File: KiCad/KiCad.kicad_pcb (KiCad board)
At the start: 2 copper layers, 39.4 x 34.8 mm, 32 parts, among them J1 Conn_01x04_Male, J2 Conn_01x04_Male, J3 Conn_01x04_Male, J4 USB_B_Micro, SW1 SW_SPDT, U1 AMS1117-3.3, U2 STM32F103C8T6, Y1 Crystal_GND24

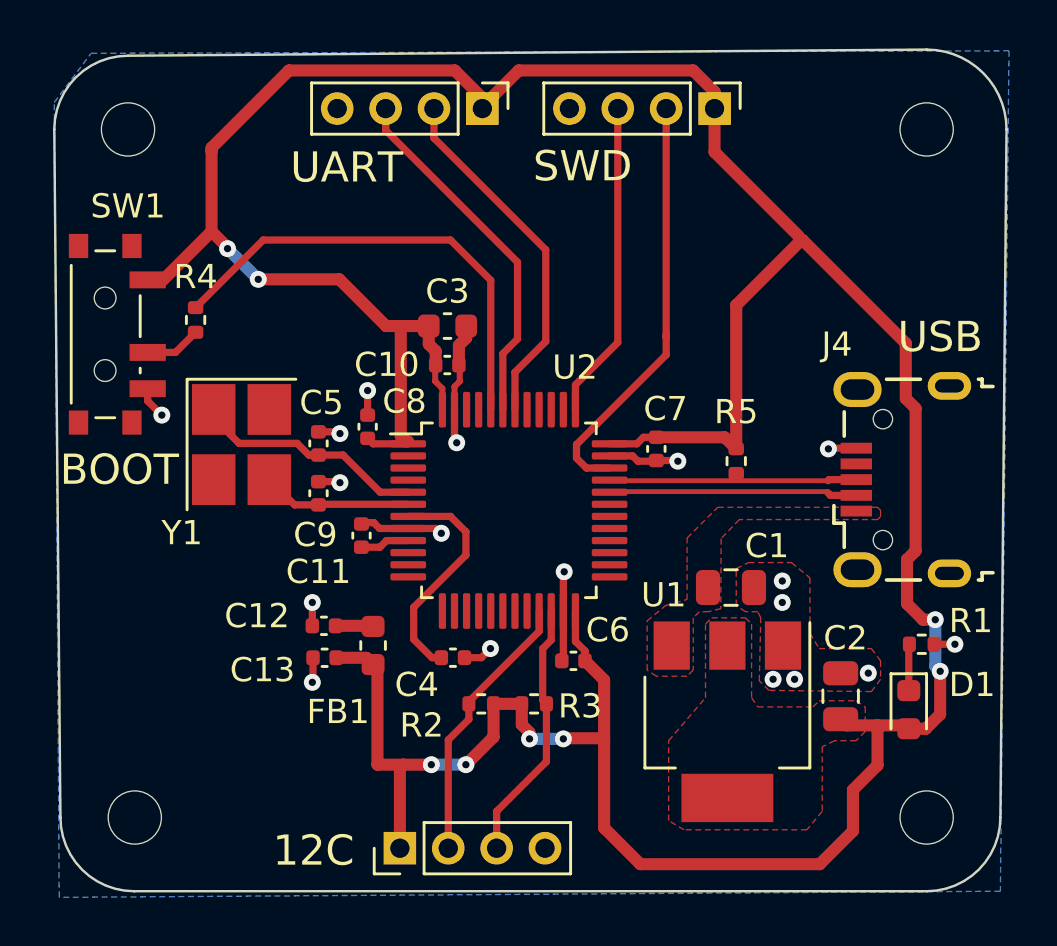
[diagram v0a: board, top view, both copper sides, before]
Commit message: Fixed some design bugs and added board title
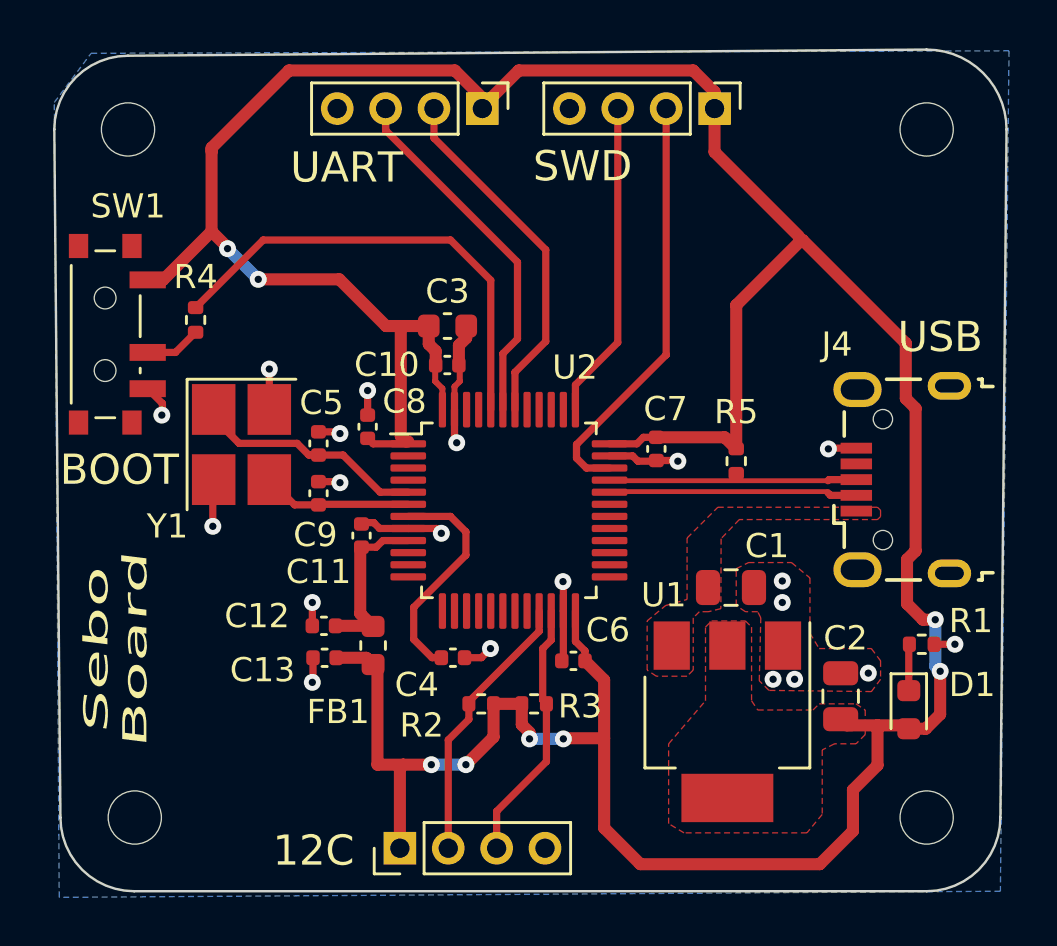
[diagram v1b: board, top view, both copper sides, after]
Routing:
- net +3.3VA: track 3.61 -> 7.13 mm
- net GND: track 24.7 -> 28.1 mm, vias 18 -> 20
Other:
- board text added: "Sebo Board"

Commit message: Sourced parts & Changed some components
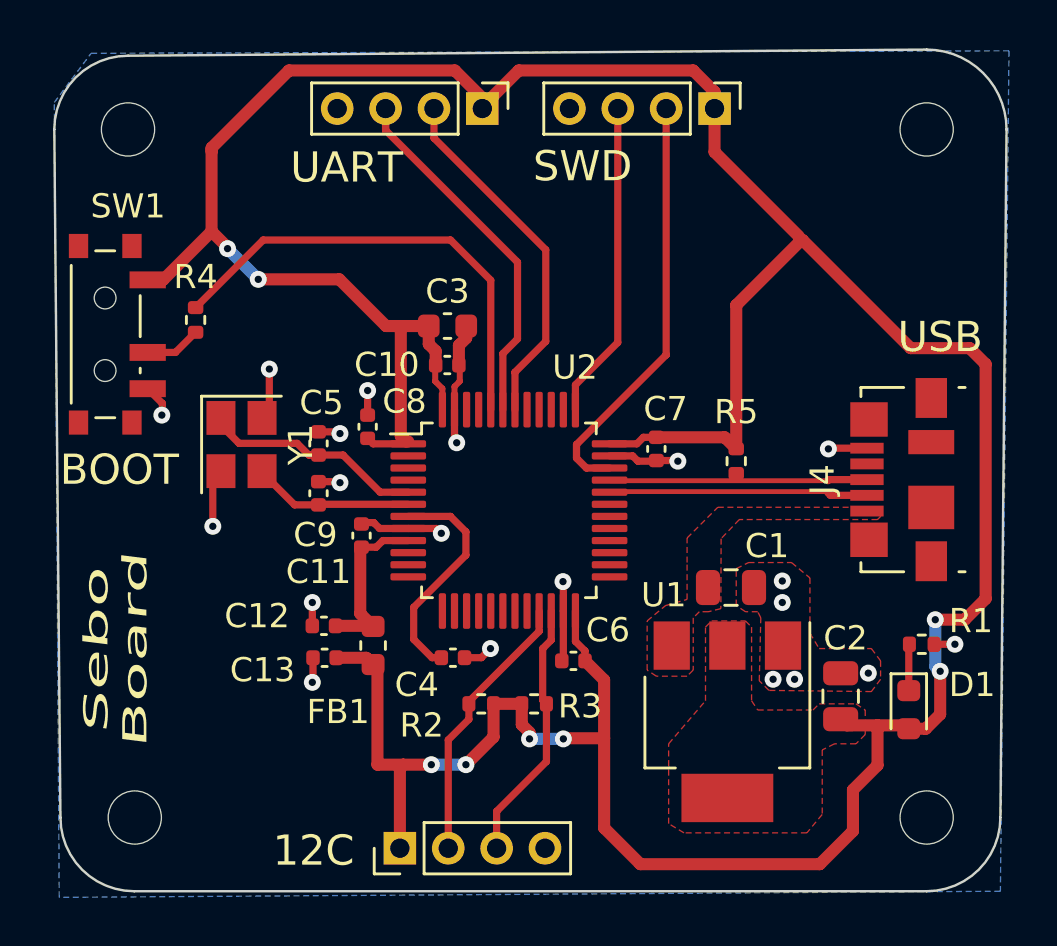
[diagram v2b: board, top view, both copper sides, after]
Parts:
- J4: footprint Connector_USB:USB_Micro-B_Wuerth_629105150521 -> Connector_USB:USB_Micro-B_Molex_47346-0001
- Y1: footprint Crystal:Crystal_SMD_3225-4Pin_3.2x2.5mm_HandSoldering -> Crystal:Crystal_SMD_3225-4Pin_3.2x2.5mm
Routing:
- net +3.3V: track 149.6 -> 152.8 mm

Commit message: Recreated the gerbers
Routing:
- net /HSE_IN: track 9.67 -> 9.10 mm
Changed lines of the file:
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@@
       (drillshape 0)
       (scaleselection 1)
-      (outputdirectory "manufacturing/")
+      (outputdirectory "manufactoringv2/gerbers/")
     )
   )
@@
     (property "Sheetname" "")
     (attr smd)
-    (fp_text reference "Y1" (at 0 -2.45 -90) (layer "F.SilkS")
+    (fp_text reference "Y1" (at 2.9232 -0.5404) (layer "F.SilkS")
       (effects (font (size 1 1) (thickness 0.15)))
     )
@@
   (segment (start 121.9745 90.158) (end 122.174 90.3575) (width 0.3) (layer "F.Cu") (net 2))
   (segment (start 122.936 83.436) (end 122.9 83.4) (width 0.25) (layer "F.Cu") (net 2))
+  (segment (start 112.762 88.138) (end 112.762 88.088) (width 0.3) (layer "F.Cu") (net 2))
   (segment (start 120.8055 90.158) (end 121.9745 90.158) (width 0.3) (layer "F.Cu") (net 2))
   (segment (start 127.218 95.568) (end 127.155 95.631) (width 0.3) (layer "F.Cu") (net 2))
@@
   (segment (start 127.218 93.5705) (end 127.218 92.3692) (width 0.3) (layer "F.Cu") (net 2))
   (segment (start 127.218 93.5705) (end 127.218 95.568) (width 0.3) (layer "F.Cu") (net 2))
-  (segment (start 112.762 88.124) (end 112.7252 88.0872) (width 0.3) (layer "F.Cu") (net 2))
+  (segment (start 112.7252 88.1248) (end 112.7252 90.0684) (width 0.3) (layer "F.Cu") (net 2))
   (segment (start 116.868 95.504) (end 116.868 96.492) (width 0.3) (layer "F.Cu") (net 2))
   (segment (start 142.5468 94.9452) (end 143.4084 94.9452) (width 0.3) (layer "F.Cu") (net 2))
@@
   (segment (start 115.062 85.238) (end 115.062 83.566) (width 0.3) (layer "F.Cu") (net 2))
   (segment (start 123.203 82.283) (end 122.9 82.586) (width 0.5) (layer "F.Cu") (net 2))
-  (segment (start 112.762 88.138) (end 112.762 88.124) (width 0.3) (layer "F.Cu") (net 2))
-  (segment (start 112.7252 88.0872) (end 112.7252 90.0684) (width 0.3) (layer "F.Cu") (net 2))
   (segment (start 131.925 87.348) (end 131.953 87.376) (width 0.3) (layer "F.Cu") (net 2))
   (segment (start 119.126 85.471) (end 119.126 84.455) (width 0.3) (layer "F.Cu") (net 2))
@@
   (segment (start 117.912 86.162) (end 117.983 86.233) (width 0.3) (layer "F.Cu") (net 2))
   (segment (start 110.6424 84.9884) (end 110.0328 84.3788) (width 0.3) (layer "F.Cu") (net 2))
+  (segment (start 112.762 88.088) (end 112.7252 88.1248) (width 0.3) (layer "F.Cu") (net 2))
   (segment (start 122.718 85.2455) (end 122.718 84.292) (width 0.25) (layer "F.Cu") (net 2))
   (segment (start 123.829 95.5) (end 124.206 95.123) (width 0.3) (layer "F.Cu") (net 2))
@@
   (segment (start 120.8055 89.658) (end 122.551 89.658) (width 0.3) (layer "F.Cu") (net 4))
   (segment (start 117.094 87.122) (end 116.696 87.122) (width 0.3) (layer "F.Cu") (net 5))
-  (segment (start 116.696 87.122) (end 116.212 86.638) (width 0.3) (layer "F.Cu") (net 5))
-  (segment (start 113.812 86.638) (end 112.762 85.588) (width 0.3) (layer "F.Cu") (net 5))
+  (segment (start 116.078 87.122) (end 115.6208 86.6648) (width 0.25) (layer "F.Cu") (net 5))
   (segment (start 119.646 88.658) (end 118.11 87.122) (width 0.3) (layer "F.Cu") (net 5))
+  (segment (start 115.6208 86.6648) (end 113.9952 86.6648) (width 0.25) (layer "F.Cu") (net 5))
+  (segment (start 113.9952 86.6648) (end 113.062 85.7316) (width 0.25) (layer "F.Cu") (net 5))
   (segment (start 118.11 87.122) (end 117.094 87.122) (width 0.3) (layer "F.Cu") (net 5))
+  (segment (start 113.062 85.7316) (end 113.062 85.588) (width 0.25) (layer "F.Cu") (net 5))
+  (segment (start 116.696 87.122) (end 116.078 87.122) (width 0.25) (layer "F.Cu") (net 5))
   (segment (start 120.8055 88.658) (end 119.646 88.658) (width 0.3) (layer "F.Cu") (net 5))
-  (segment (start 116.212 86.638) (end 113.812 86.638) (width 0.3) (layer "F.Cu") (net 5))
-  (segment (start 112.762 85.588) (end 112.762 85.238) (width 0.3) (layer "F.Cu") (net 5))
   (segment (start 117.094 89.182) (end 116.106 89.182) (width 0.3) (layer "F.Cu") (net 6))
   (segment (start 120.8055 89.158) (end 117.118 89.158) (width 0.3) (layer "F.Cu") (net 6))
